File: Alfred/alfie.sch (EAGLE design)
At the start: 19 parts, among them IC1 7805TV, K1 G6A-234P, K2 G6A-234P

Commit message: Added diodes and resistors.
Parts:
- added D5, D6: 1N4148DO35-7, diode:1N4148DO35-7
- added R1: (no value), rcl:R-EU_0207/10
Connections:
- net +5V: now also D5.C, D6.C
- net DOORBELL: now also R1.2
- net GND: now also R1.1
- net N$1: now also D6.A
- net N$2: now also D5.A
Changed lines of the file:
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@@
 <grid distance="0.1" unitdist="inch" unit="inch" style="lines" multiple="1" display="no" altdistance="0.01" altunitdist="inch" altunit="inch"/>
 <layers>
-<layer number="1" name="Top" color="4" fill="1" visible="yes" active="no"/>
-<layer number="16" name="Bottom" color="1" fill="1" visible="yes" active="no"/>
-<layer number="17" name="Pads" color="2" fill="1" visible="yes" active="no"/>
-<layer number="18" name="Vias" color="2" fill="1" visible="yes" active="no"/>
-<layer number="19" name="Unrouted" color="6" fill="1" visible="yes" active="no"/>
-<layer number="20" name="Dimension" color="15" fill="1" visible="yes" active="no"/>
-<layer number="21" name="tPlace" color="7" fill="1" visible="yes" active="no"/>
-<layer number="22" name="bPlace" color="7" fill="1" visible="yes" active="no"/>
-<layer number="23" name="tOrigins" color="15" fill="1" visible="yes" active="no"/>
-<layer number="24" name="bOrigins" color="15" fill="1" visible="yes" active="no"/>
-<layer number="25" name="tNames" color="7" fill="1" visible="yes" active="no"/>
-<layer number="26" name="bNames" color="7" fill="1" visible="yes" active="no"/>
-<layer number="27" name="tValues" color="7" fill="1" visible="yes" active="no"/>
-<layer number="28" name="bValues" color="7" fill="1" visible="yes" active="no"/>
+<layer number="1" name="Top" color="4" fill="1" visible="no" active="no"/>
+<layer number="16" name="Bottom" color="1" fill="1" visible="no" active="no"/>
+<layer number="17" name="Pads" color="2" fill="1" visible="no" active="no"/>
+<layer number="18" name="Vias" color="2" fill="1" visible="no" active="no"/>
+<layer number="19" name="Unrouted" color="6" fill="1" visible="no" active="no"/>
+<layer number="20" name="Dimension" color="15" fill="1" visible="no" active="no"/>
+<layer number="21" name="tPlace" color="7" fill="1" visible="no" active="no"/>
+<layer number="22" name="bPlace" color="7" fill="1" visible="no" active="no"/>
+<layer number="23" name="tOrigins" color="15" fill="1" visible="no" active="no"/>
+<layer number="24" name="bOrigins" color="15" fill="1" visible="no" active="no"/>
+<layer number="25" name="tNames" color="7" fill="1" visible="no" active="no"/>
+<layer number="26" name="bNames" color="7" fill="1" visible="no" active="no"/>
+<layer number="27" name="tValues" color="7" fill="1" visible="no" active="no"/>
+<layer number="28" name="bValues" color="7" fill="1" visible="no" active="no"/>
 <layer number="29" name="tStop" color="7" fill="3" visible="no" active="no"/>
 <layer number="30" name="bStop" color="7" fill="6" visible="no" active="no"/>
@@
 <layer number="35" name="tGlue" color="7" fill="4" visible="no" active="no"/>
 <layer number="36" name="bGlue" color="7" fill="5" visible="no" active="no"/>
-<layer number="37" name="tTest" color="7" fill="1" visible="yes" active="no"/>
-<layer number="38" name="bTest" color="7" fill="1" visible="yes" active="no"/>
+<layer number="37" name="tTest" color="7" fill="1" visible="no" active="no"/>
+<layer number="38" name="bTest" color="7" fill="1" visible="no" active="no"/>
 <layer number="39" name="tKeepout" color="4" fill="11" visible="no" active="no"/>
 <layer number="40" name="bKeepout" color="1" fill="11" visible="no" active="no"/>
@@
 <layer number="44" name="Drills" color="7" fill="1" visible="no" active="no"/>
 <layer number="45" name="Holes" color="7" fill="1" visible="no" active="no"/>
-<layer number="46" name="Milling" color="3" fill="1" visible="yes" active="no"/>
-<layer number="47" name="Measures" color="7" fill="1" visible="yes" active="no"/>
-<layer number="48" name="Document" color="7" fill="1" visible="yes" active="no"/>
-<layer number="49" name="Reference" color="7" fill="1" visible="yes" active="no"/>
-<layer number="51" name="tDocu" color="7" fill="1" visible="yes" active="no"/>
-<layer number="52" name="bDocu" color="7" fill="1" visible="yes" active="no"/>
+<layer number="46" name="Milling" color="3" fill="1" visible="no" active="no"/>
+<layer number="47" name="Measures" color="7" fill="1" visible="no" active="no"/>
+<layer number="48" name="Document" color="7" fill="1" visible="no" active="no"/>
+<layer number="49" name="Reference" color="7" fill="1" visible="no" active="no"/>
+<layer number="51" name="tDocu" color="7" fill="1" visible="no" active="no"/>
+<layer number="52" name="bDocu" color="7" fill="1" visible="no" active="no"/>
 <layer number="91" name="Nets" color="2" fill="1" visible="yes" active="yes"/>
 <layer number="92" name="Busses" color="1" fill="1" visible="yes" active="yes"/>
@@
 <part name="GND7" library="supply1" deviceset="GND" device=""/>
 <part name="GND8" library="supply1" deviceset="GND" device=""/>
+<part name="D5" library="diode" deviceset="1N4148" device="DO35-7"/>
+<part name="D6" library="diode" deviceset="1N4148" device="DO35-7"/>
+<part name="R1" library="rcl" deviceset="R-EU_" device="0207/10"/>
 </parts>
 <sheets>
@@
 <instance part="GND7" gate="1" x="27.94" y="-53.34"/>
 <instance part="GND8" gate="1" x="27.94" y="-78.74"/>
+<instance part="D5" gate="G$1" x="121.92" y="-45.72" rot="R90"/>
+<instance part="D6" gate="G$1" x="121.92" y="-5.08" rot="R90"/>
+<instance part="R1" gate="G$1" x="177.8" y="73.66" rot="R90"/>
 </instances>
 <busses>
@@
 <pinref part="K1" gate="1" pin="1"/>
 <pinref part="P+3" gate="1" pin="+5V"/>
+<pinref part="D6" gate="G$1" pin="C"/>
+<wire x1="121.92" y1="-2.54" x2="121.92" y2="0" width="0.1524" layer="91"/>
+<wire x1="121.92" y1="0" x2="129.54" y2="0" width="0.1524" layer="91"/>
+<junction x="129.54" y="0"/>
 </segment>
 <segment>
 <pinref part="K2" gate="1" pin="1"/>
 <pinref part="P+4" gate="1" pin="+5V"/>
+<pinref part="D5" gate="G$1" pin="C"/>
+<wire x1="129.54" y1="-40.64" x2="121.92" y2="-40.64" width="0.1524" layer="91"/>
+<wire x1="121.92" y1="-40.64" x2="121.92" y2="-43.18" width="0.1524" layer="91"/>
+<junction x="129.54" y="-40.64"/>
 </segment>
 </net>
@@
 <wire x1="170.18" y1="68.58" x2="157.48" y2="68.58" width="0.1524" layer="91"/>
 <junction x="157.48" y="68.58"/>
+<pinref part="R1" gate="G$1" pin="1"/>
+<wire x1="177.8" y1="68.58" x2="170.18" y2="68.58" width="0.1524" layer="91"/>
+<junction x="170.18" y="68.58"/>
 </segment>
 <segment>
@@
 <pinref part="IC1" gate="A1" pin="VO"/>
 <wire x1="167.64" y1="78.74" x2="170.18" y2="78.74" width="0.1524" layer="91"/>
-<label x="177.8" y="78.74" size="1.27" layer="95" xref="yes"/>
+<label x="182.88" y="78.74" size="1.27" layer="95" xref="yes"/>
 <pinref part="C2" gate="G$1" pin="1"/>
 <wire x1="170.18" y1="78.74" x2="177.8" y2="78.74" width="0.1524" layer="91"/>
 <junction x="170.18" y="78.74"/>
+<pinref part="R1" gate="G$1" pin="2"/>
+<wire x1="177.8" y1="78.74" x2="182.88" y2="78.74" width="0.1524" layer="91"/>
+<junction x="177.8" y="78.74"/>
 </segment>
 <segment>
@@
 <pinref part="K1" gate="1" pin="2"/>
 <pinref part="U$2" gate="G$1" pin="D"/>
+<pinref part="D6" gate="G$1" pin="A"/>
+<wire x1="121.92" y1="-7.62" x2="121.92" y2="-10.16" width="0.1524" layer="91"/>
+<wire x1="121.92" y1="-10.16" x2="129.54" y2="-10.16" width="0.1524" layer="91"/>
+<junction x="129.54" y="-10.16"/>
 </segment>
 </net>
@@
 <pinref part="K2" gate="1" pin="2"/>
 <pinref part="U$5" gate="G$1" pin="D"/>
-</segment>
-</net>
+<pinref part="D5" gate="G$1" pin="A"/>
+<wire x1="129.54" y1="-50.8" x2="121.92" y2="-50.8" width="0.1524" layer="91"/>
+<wire x1="121.92" y1="-50.8" x2="121.92" y2="-48.26" width="0.1524" layer="91"/>
+<junction x="129.54" y="-50.8"/>
+</segment>
+</net>

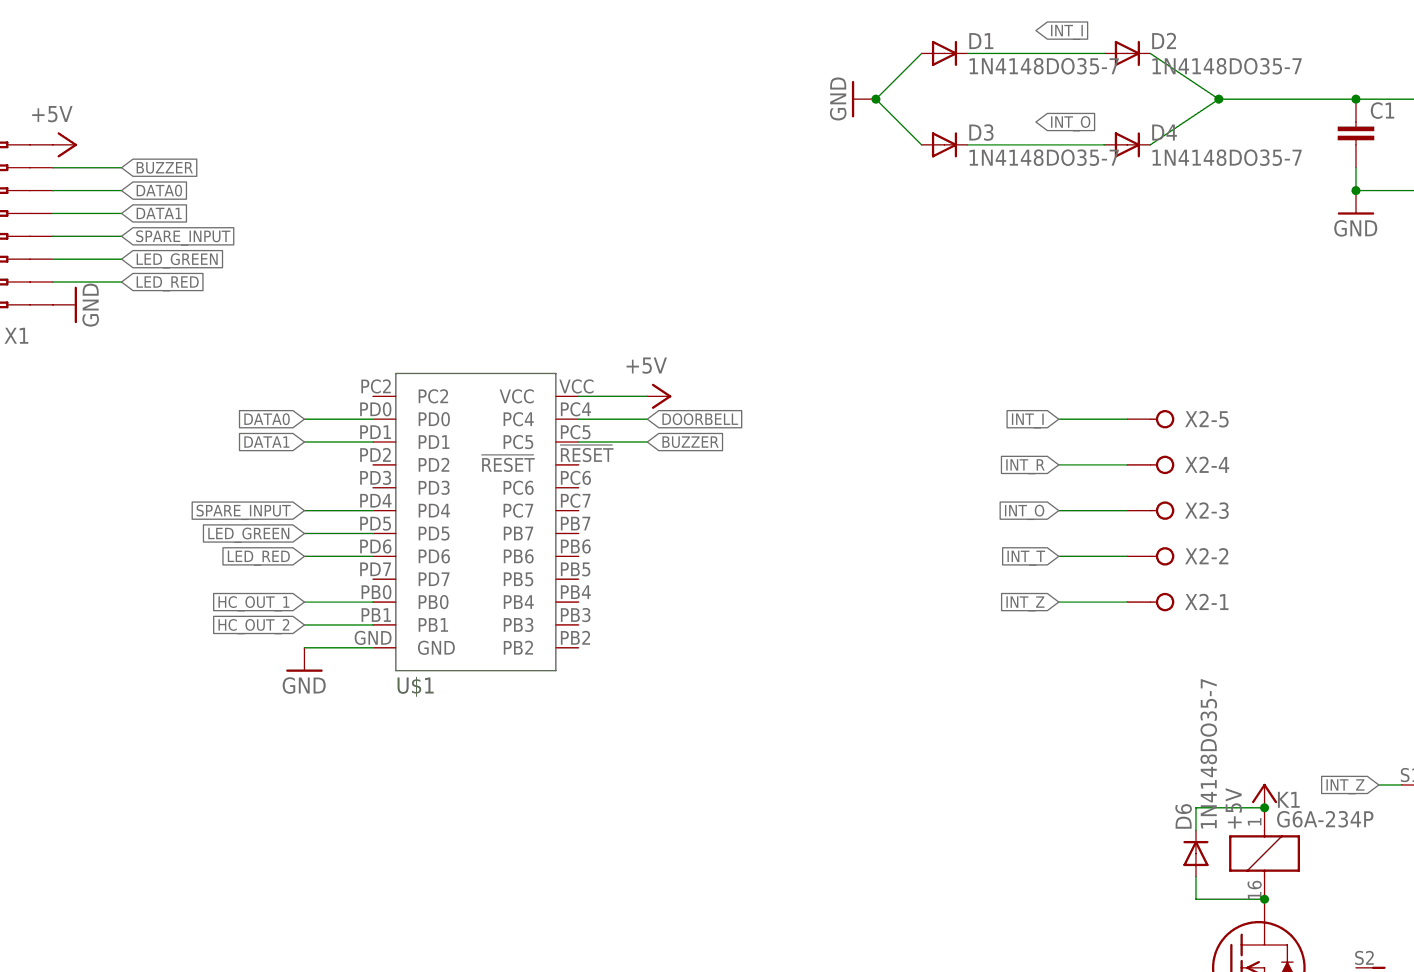
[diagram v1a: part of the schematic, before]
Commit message: Added expansion header, re routed the FETs a little
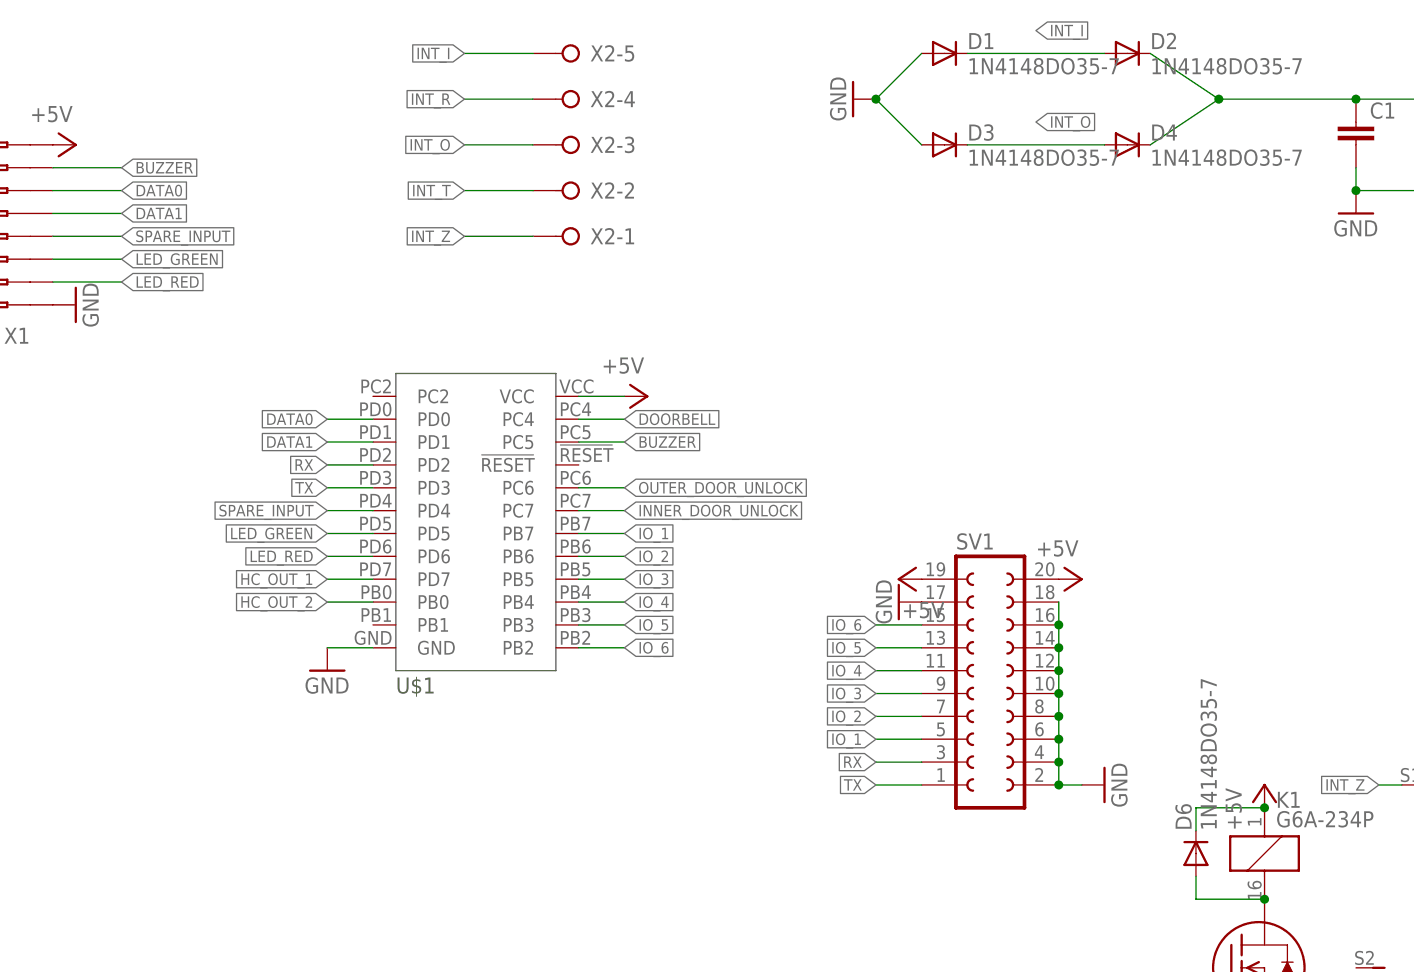
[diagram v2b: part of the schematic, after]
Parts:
- added SV1: (no value), con-lsta:FE10-2
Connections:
- new net IO_1: SV1.5, U$1.PB7
- new net IO_2: SV1.7, U$1.PB6
- new net IO_3: SV1.9, U$1.PB5
- new net IO_4: SV1.11, U$1.PB4
- new net IO_5: SV1.13, U$1.PB3
- new net IO_6: SV1.15, U$1.PB2
- new net RX: SV1.3, U$1.PD2
- new net TX: SV1.1, U$1.PD3
- net +5V: now also SV1.19, SV1.20
- net GND: now also SV1.10, SV1.12, SV1.14, SV1.16, SV1.17, SV1.18, SV1.2, SV1.4, SV1.6, SV1.8
- net HC_OUT_1: now also U$1.PD7; no longer U$1.PB0
- net HC_OUT_2: now also U$1.PB0; no longer U$1.PB1
- net INNER_DOOR_UNLOCK: now also U$1.PC7
- net OUTER_DOOR_UNLOCK: now also U$1.PC6
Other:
- moved on the sheet: X2-1, X2-2, X2-3, X2-4, X2-5

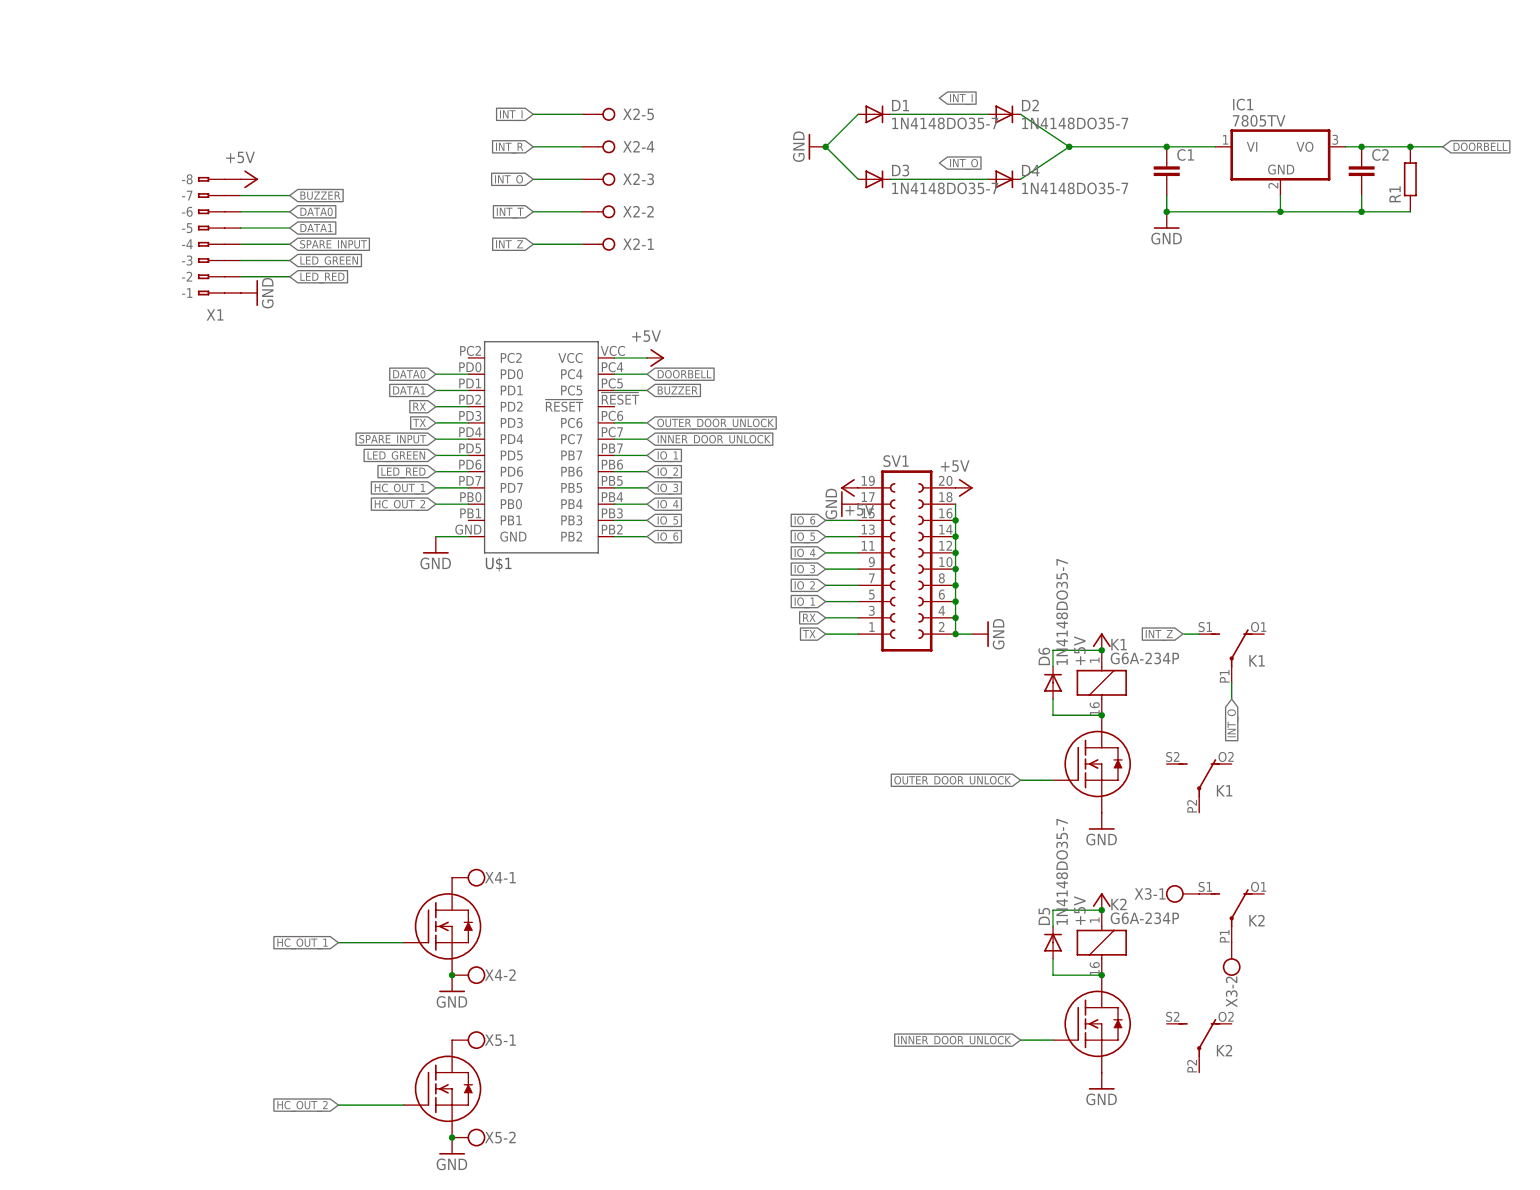
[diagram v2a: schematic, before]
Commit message: Added decoupling, tidied up schematic
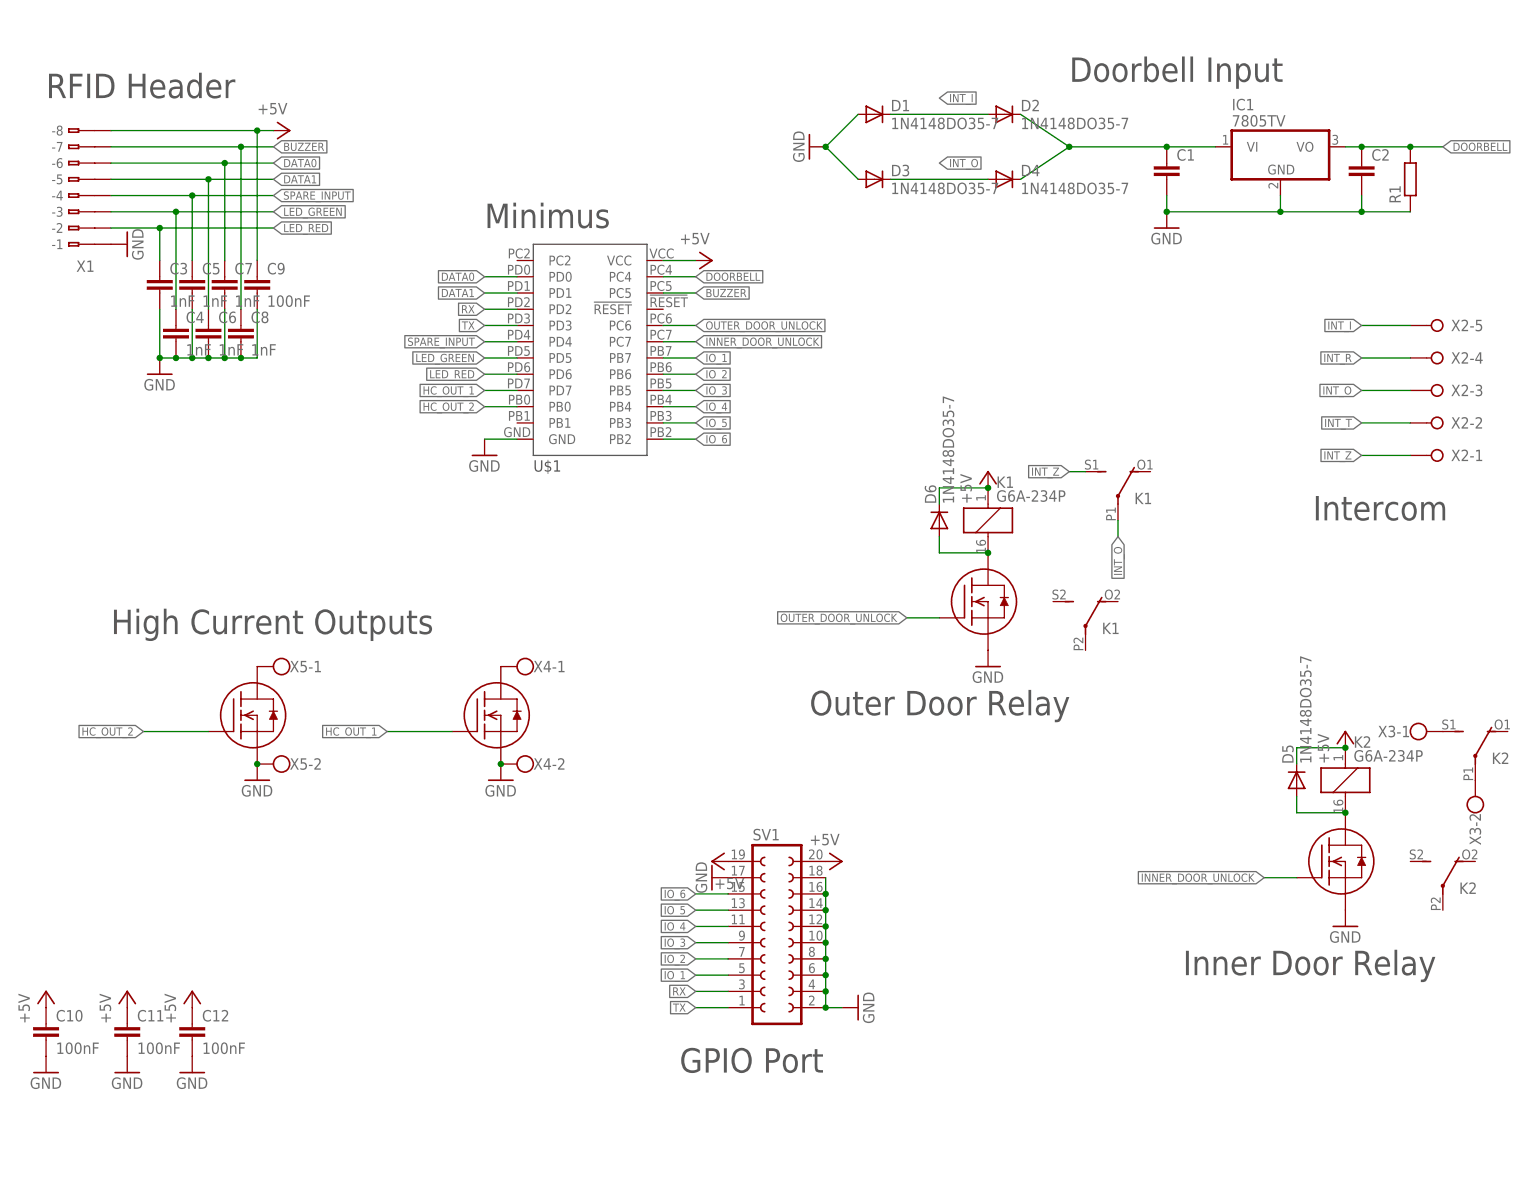
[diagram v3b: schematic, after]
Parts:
- added C10, C11, C12, C9: 100nF, rcl:C-EUC0805
- added C3, C4, C5, C6, C7, C8: 1nF, rcl:C-EUC0805
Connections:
- net +5V: now also C10.1, C11.1, C12.1, C9.1
- net BUZZER: now also C8.1
- net DATA0: now also C7.1
- net DATA1: now also C6.1
- net GND: now also C10.2, C11.2, C12.2, C3.2, C4.2, C5.2, C6.2, C7.2, C8.2, C9.2
- net LED_GREEN: now also C4.1
- net LED_RED: now also C3.1
- net SPARE_INPUT: now also C5.1
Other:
- note added: "Doorbell Input"
- note added: "GPIO Port"
- note added: "High Current Outputs"
- note added: "Inner Door Relay"
- note added: "Intercom"
- note added: "Minimus"
- note added: "Outer Door Relay"
- note added: "RFID Header"
- moved on the sheet: D5, D6, K1, K2, SV1, U$1, X1, X2-1, X2-2, X2-3, X2-4, X2-5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
